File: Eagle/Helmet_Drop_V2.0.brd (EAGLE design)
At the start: 172.7 x 106.4 mm, 27 parts, among them Q3 MOSFET-NCH, Q4 MOSFET-NCH, Q5 MOSFET-NCH, U1 TH_DS_LIBRARIES_ITSYBITSY_5V, X1 MSTBA4

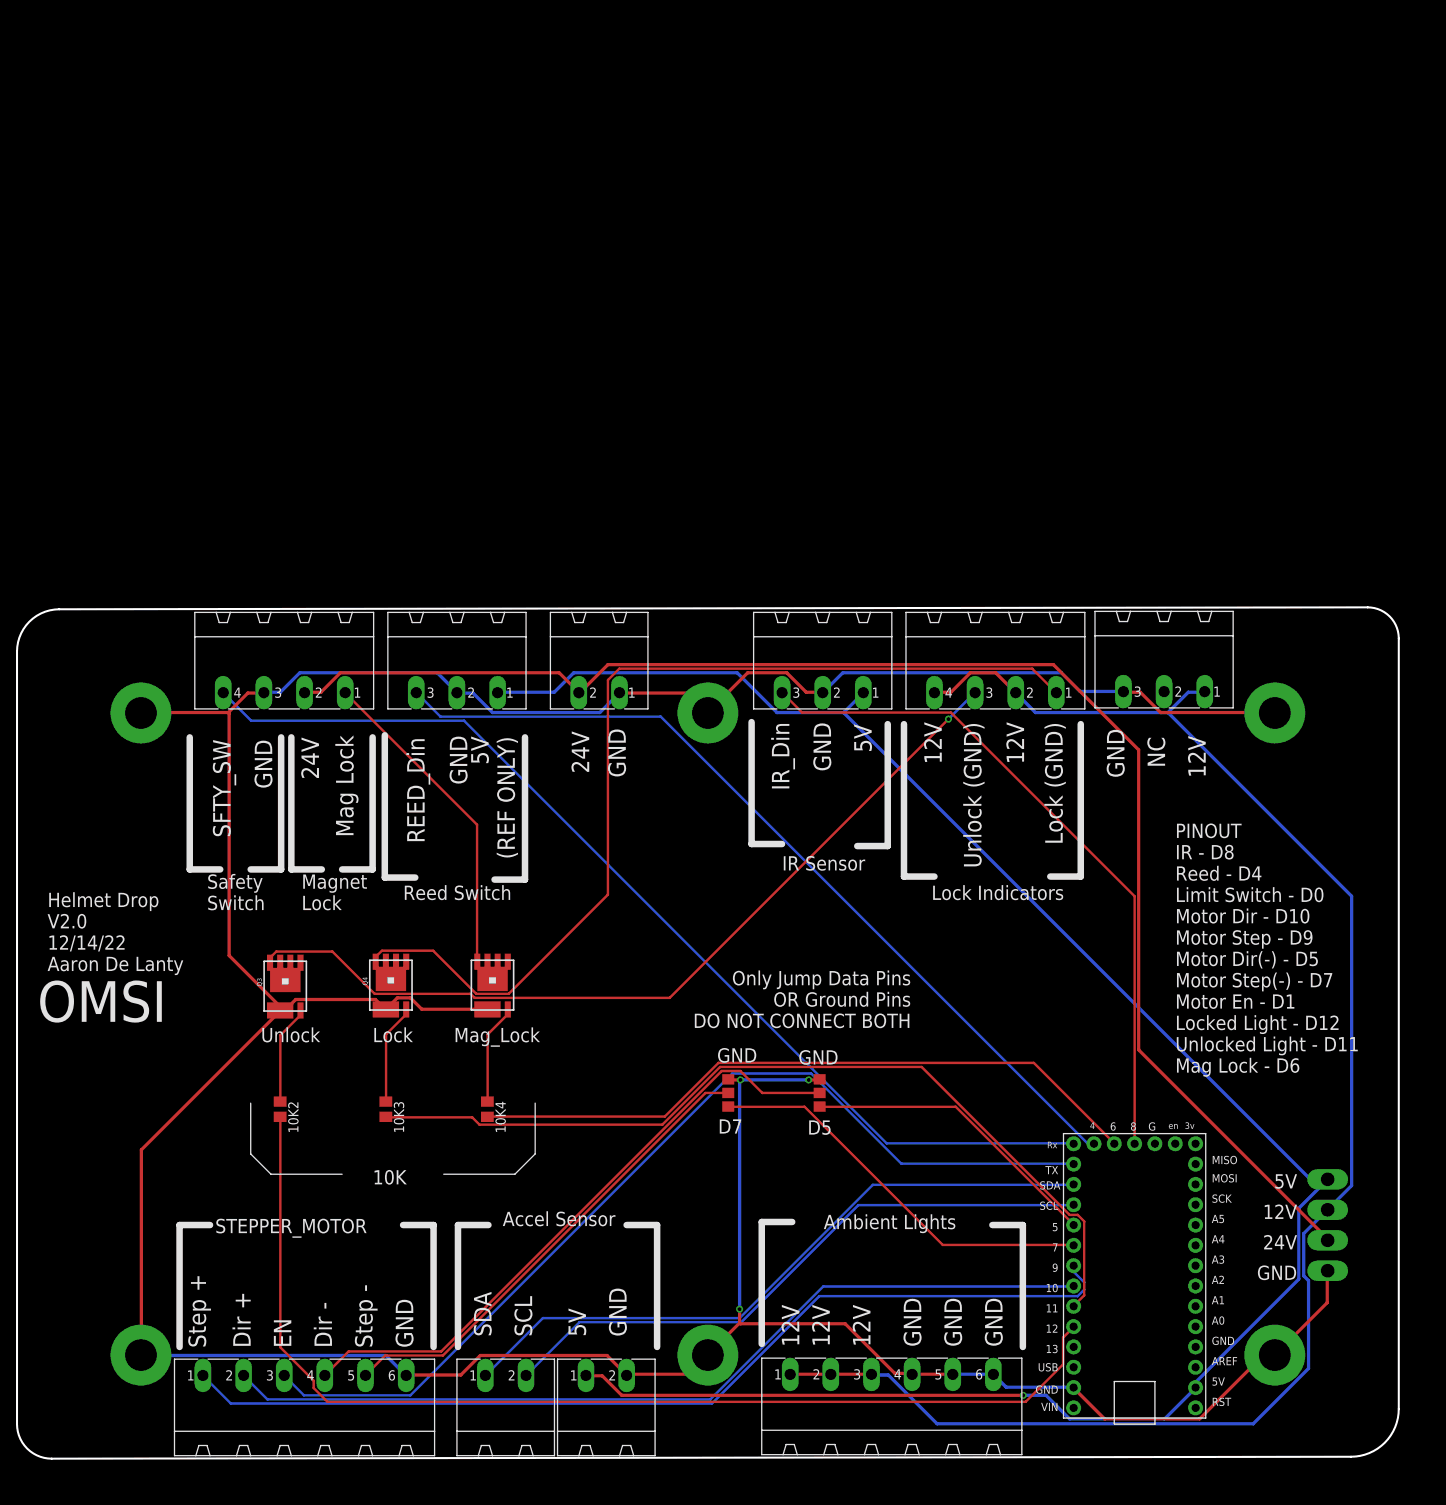
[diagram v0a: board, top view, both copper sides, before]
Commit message: Moved connectors for ease of access
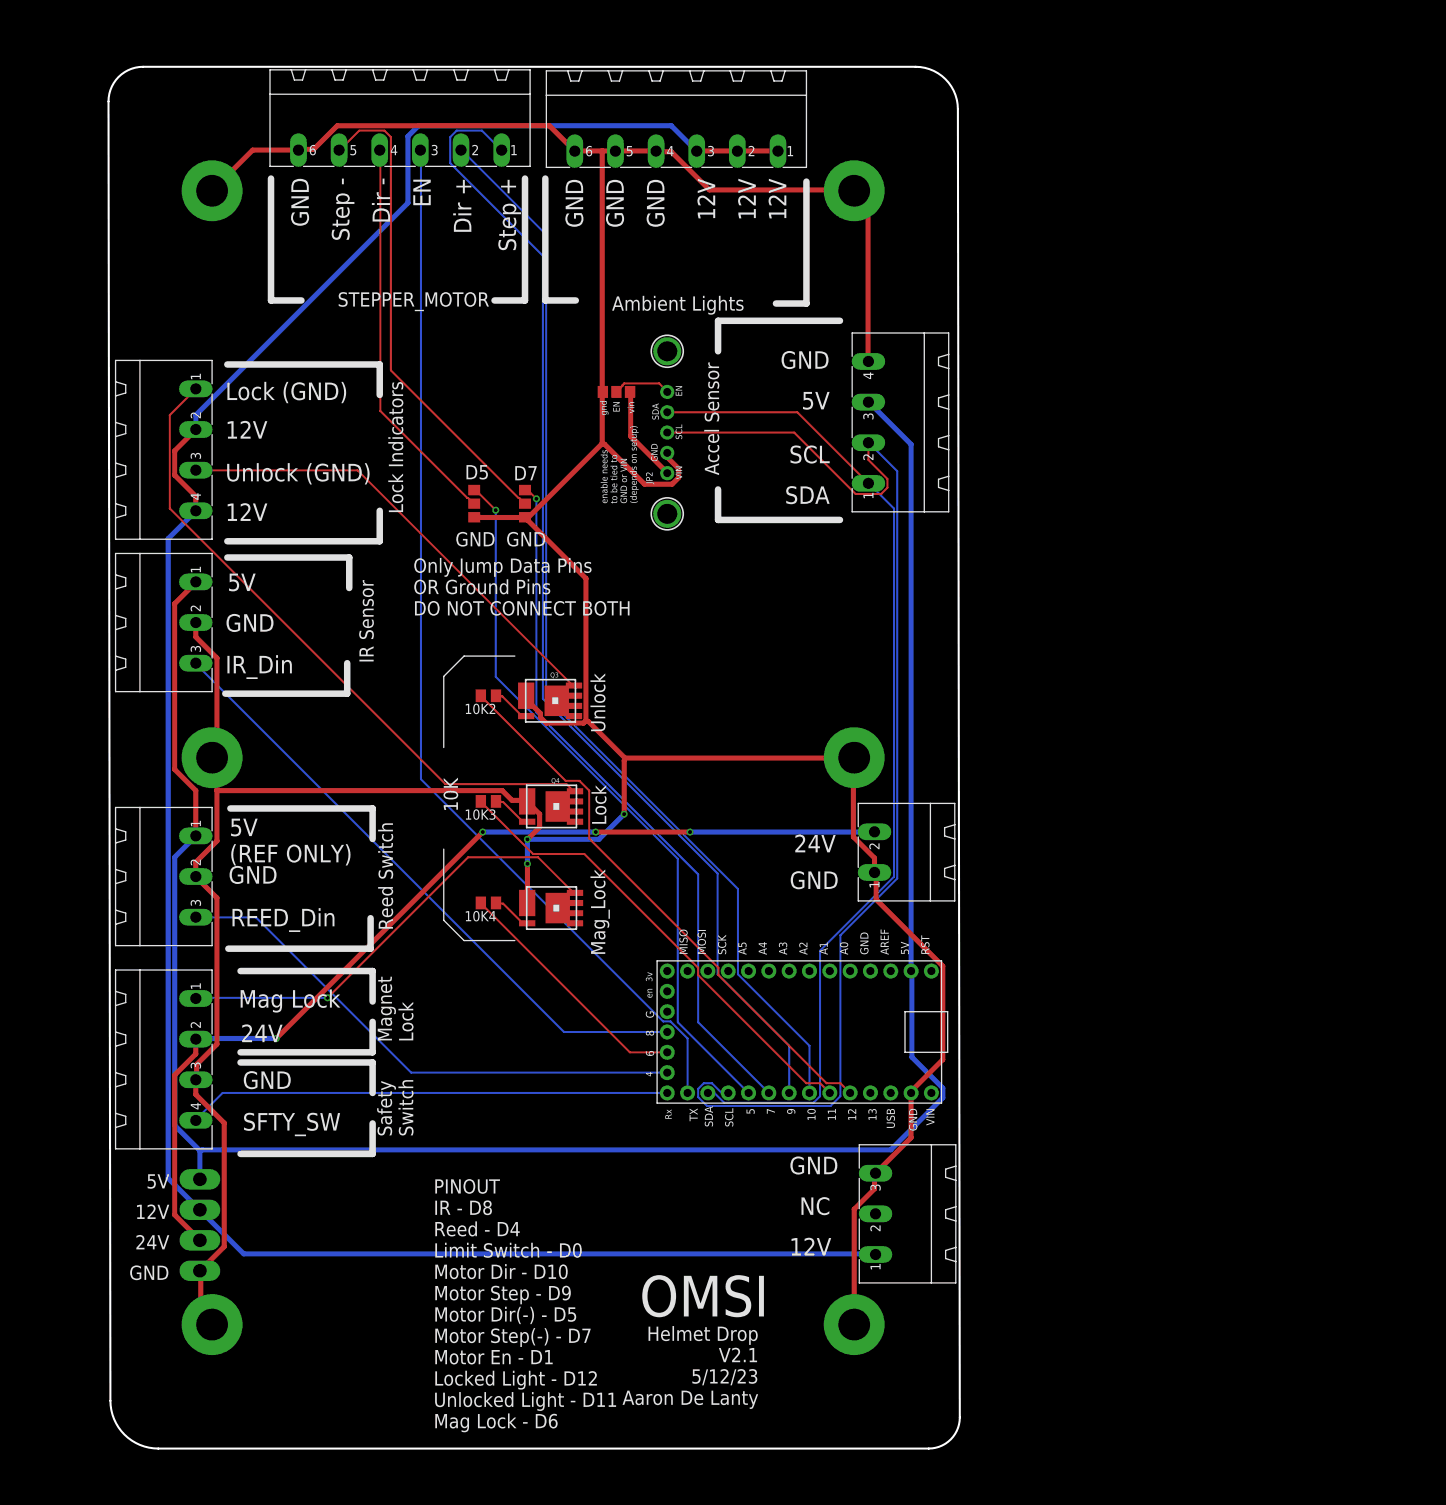
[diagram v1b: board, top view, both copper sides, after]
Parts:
- removed 5V_IN, SDA_SCL: MSTBA2, th_libraries:MSTBA2
- added JMP3: 0R-JUMPA, jump-0r-smd:A0R-JMP
- added JP2: (no value), microbuilder:1X05_ROUND_70
- added U$19, U$21: MOUNTINGHOLE2.5, microbuilder:MOUNTINGHOLE_2.5_PLATED
- added X2: TH_DS_LIBRARIES_MSTBA4, OMSI_Default_V1:TH_DS_LIBRARIES_MSTBA4
- moved AUXILLARY_LIGHTS1 165.3 mm to (82.4, 168.5), turned to 180 degrees
- moved STEPPER_MOTOR 163.8 mm to (47.9, 168.7), turned to 180 degrees
- moved S9 145.8 mm to (24.4, 158.5), turned to 270 degrees
- moved TP1 141.0 mm to (22.9, 25.4)
- moved TP2 141.0 mm to (22.9, 33.0)
- moved S11 132.9 mm to (24.4, 16.8), turned to 270 degrees
- moved S5 110.5 mm to (104.6, 158.5), turned to 270 degrees
- moved LOCK_LIGHTS 108.0 mm to (17.3, 126.1), turned to 270 degrees
- moved S7 97.0 mm to (24.4, 87.6), turned to 270 degrees
- moved S12 92.8 mm to (104.6, 16.8), turned to 270 degrees
- moved JMP1 85.4 mm to (57.1, 119.4), turned to 180 degrees
- moved IR_IN 83.5 mm to (17.3, 104.5), turned to 270 degrees
- moved JMP2 77.9 mm to (63.5, 119.4), turned to 180 degrees
- moved 12V_IN 76.9 mm to (112.4, 30.6), turned to 90 degrees
- moved 10K2 57.9 mm to (58.9, 95.4), turned to 180 degrees
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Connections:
- removed net D2: SDA_SCL.1, U1.SDA
- removed net D3: SDA_SCL.2, U1.SCL
- new net EN: JMP3.2, JP2.5
- new net SCL: JP2.3, U1.SCL, X2.2
- new net SDA: JP2.4, U1.SDA, X2.1
- new net VCC: JMP3.1, JP2.1
- net 5V: now also X2.3; no longer 5V_IN.1
- net GND: now also JMP3.3, JP2.2, X2.4; no longer 5V_IN.2
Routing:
- net SCL: track 0.00 -> 148.1 mm
- net SDA: track 0.00 -> 125.5 mm
- net D2: track 83.4 -> 0.00 mm
- net 12V: track 202.5 -> 285.4 mm
- net D3: track 77.3 -> 0.00 mm
- net D0: track 129.7 -> 60.4 mm
- net D12: track 137.2 -> 70.8 mm
- net 24V: track 183.3 -> 123.2 mm, vias 0 -> 4
- net N$1: track 85.4 -> 31.1 mm
- net D5: track 37.9 -> 89.7 mm, vias 0 -> 1
- net D11: track 109.9 -> 59.3 mm
- net N$7: track 107.3 -> 58.5 mm, vias 1 -> 0
- net D4: track 108.1 -> 67.0 mm
- net N$10: track 122.0 -> 81.6 mm
- net D7: track 50.4 -> 88.2 mm, vias 0 -> 1
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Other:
- board size 172.7 x 106.4 mm -> 106.4 x 172.7 mm
- board text added: "Helmet Drop V2.1 5/12/23 Aaron De Lanty"
- board text added: "VIN"
- board text added: "enable needs to be tied to GND or VIN (depends on setup)"
- board text added: "gnd"
- board text added: "vin"
- board text removed: "Helmet Drop V2.0 12/14/22 Aaron De Lanty"

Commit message: board fix
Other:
- board text added: "Only Jump Data Pins OR Ground Pins DO NOT CONNECT BOTH Default should be DATA"
- board text removed: "Only Jump Data Pins OR Ground Pins DO NOT CONNECT BOTH"
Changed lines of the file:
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@@
 <text x="49.53" y="105.41" size="1.778" layer="25">Only Jump Data Pins
 OR Ground Pins
-DO NOT CONNECT BOTH</text>
+DO NOT CONNECT BOTH
+Default should be DATA</text>
 <text x="19.05" y="31.75" size="1.778" layer="25" rot="R180">12V</text>
 <text x="102.362" y="77.978" size="2.1844" layer="25" rot="R180">24V</text>

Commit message: update
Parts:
- added X3: PHOENIX_508_2PIN, OMSI_Default_V1:PHOENIX_508_2PIN
- U1: value TH_DS_LIBRARIES_ITSYBITSY_5V -> ADAFRUIT_ITSYBITSY_5V; device Helmet_Drop_V1.5:TH_DS_LIBRARIES_ADAFRUIT_LENOARDO -> OMSI_Default_V1:ADAFRUIT_ITSYBITSY
- moved 24V 45.7 mm to (112.4, 30.1)
- moved 12V_IN 45.0 mm to (112.3, 75.6)
- moved U1 5.11 mm to (97.9, 52.1)
- moved X2 2.54 mm to (111.5, 127.0)
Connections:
- new net N$2: U1.D13, X3.2
- net GND: now also X3.1
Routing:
- net N$2: track 0.00 -> 62.1 mm
- net SCL: track 148.1 -> 112.1 mm
- net GND: track 504.6 -> 534.8 mm, vias 3 -> 4
- net D10: track 135.9 -> 153.9 mm
- net 12V: track 285.4 -> 301.1 mm
- net D9: track 144.8 -> 134.1 mm, vias 0 -> 1
- net 24V: track 123.2 -> 114.2 mm, vias 4 -> 0
- net SDA: track 125.5 -> 119.7 mm
- net D12: track 70.8 -> 74.4 mm
- net N$21: track 56.6 -> 53.5 mm, vias 1 -> 0
- net 5V: track 265.7 -> 263.5 mm
- net D1: track 132.3 -> 133.6 mm
- net D5: track 89.7 -> 91.0 mm, vias 1 -> 2
- net D7: track 88.2 -> 89.4 mm
- net D11: track 59.3 -> 60.0 mm
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- added copper zone on layer 1, net GND
- added copper zone on layer 16, net GND
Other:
- board text added: "Home_in"
- board text added: "PINOUT IR - D8 Reed - D4 Limit Switch - D0 Motor Dir - D10 Motor Step - D9 Motor Dir(-) - D5 Motor Step(-) - D7 Motor En - D1 Locked Light - D12 Unlocked Light - D11 Mag Lock - D6 Home Switch - D13"
- board text removed: "PINOUT IR - D8 Reed - D4 Limit Switch - D0 Motor Dir - D10 Motor Step - D9 Motor Dir(-) - D5 Motor Step(-) - D7 Motor En - D1 Locked Light - D12 Unlocked Light - D11 Mag Lock - D6"
